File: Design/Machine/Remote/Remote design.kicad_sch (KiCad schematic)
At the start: 27 parts, among them SW1 PAuto, SW10 SyncRemote, SW11 PManual, SW12 YCardR, SW13 RCardR, SW14 IncPeriod, SW15 DecRight, SW16 IncRight, SW17 ThreeMin, SW18 DecTime, SW19 CycleTime, SW2 Block, SW20 PauseRes, SW21 Upload, SW3 YCardL, SW4 RCardL, SW5 DecLeft, SW6 IncLeft, SW7 OneMin, SW8 IncTime, SW9 ResetMachine

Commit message: fix: RF module PCB footprint
change RF module's PCB footprint
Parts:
- FS1000A1: footprint Connector_PinSocket_2.54mm:PinSocket_1x03_P2.54mm_Vertical -> Arduino_modules:FS1000A_Straight-Pins_Without-Headers
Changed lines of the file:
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@@
       (effects (font (size 1.27 1.27)) (justify left))
     )
-    (property "Footprint" "Connector_PinSocket_2.54mm:PinSocket_1x03_P2.54mm_Vertical" (at 254 104.14 0)
+    (property "Footprint" "Arduino_modules:FS1000A_Straight-Pins_Without-Headers" (at 254 104.14 0)
       (effects (font (size 1.27 1.27)) hide)
     )

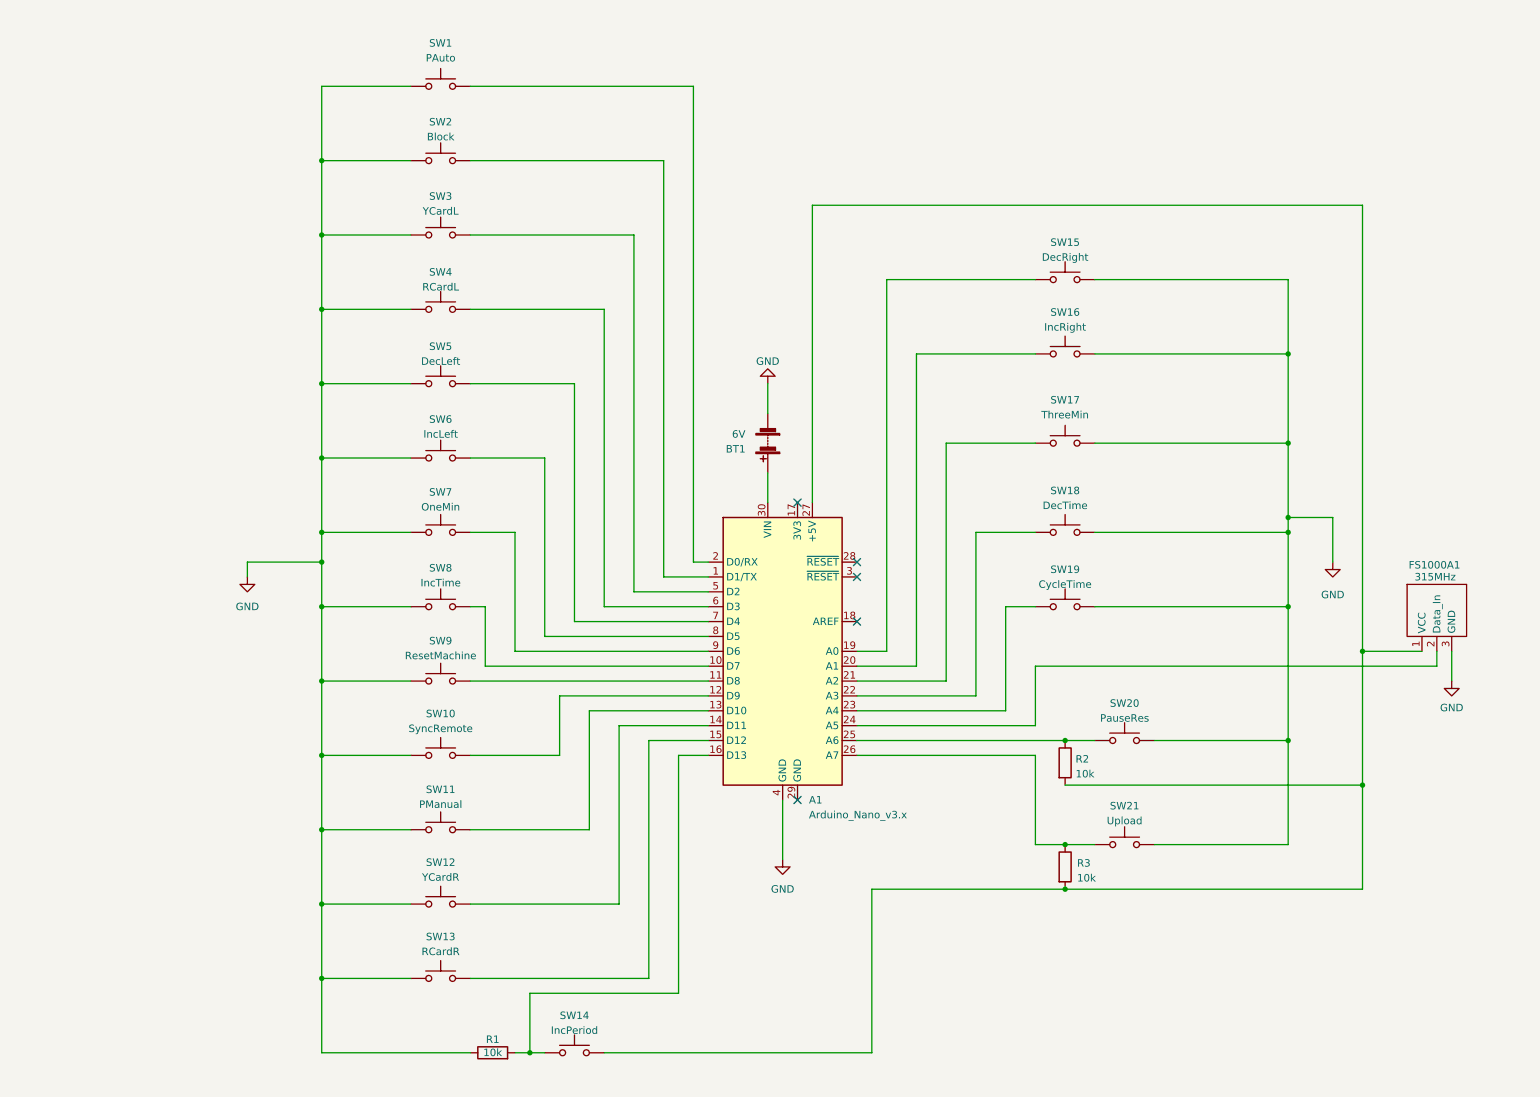
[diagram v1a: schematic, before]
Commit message: fix: controller schematic
fix controller's connections to GND and VCC, add SPST ON/OFF switch
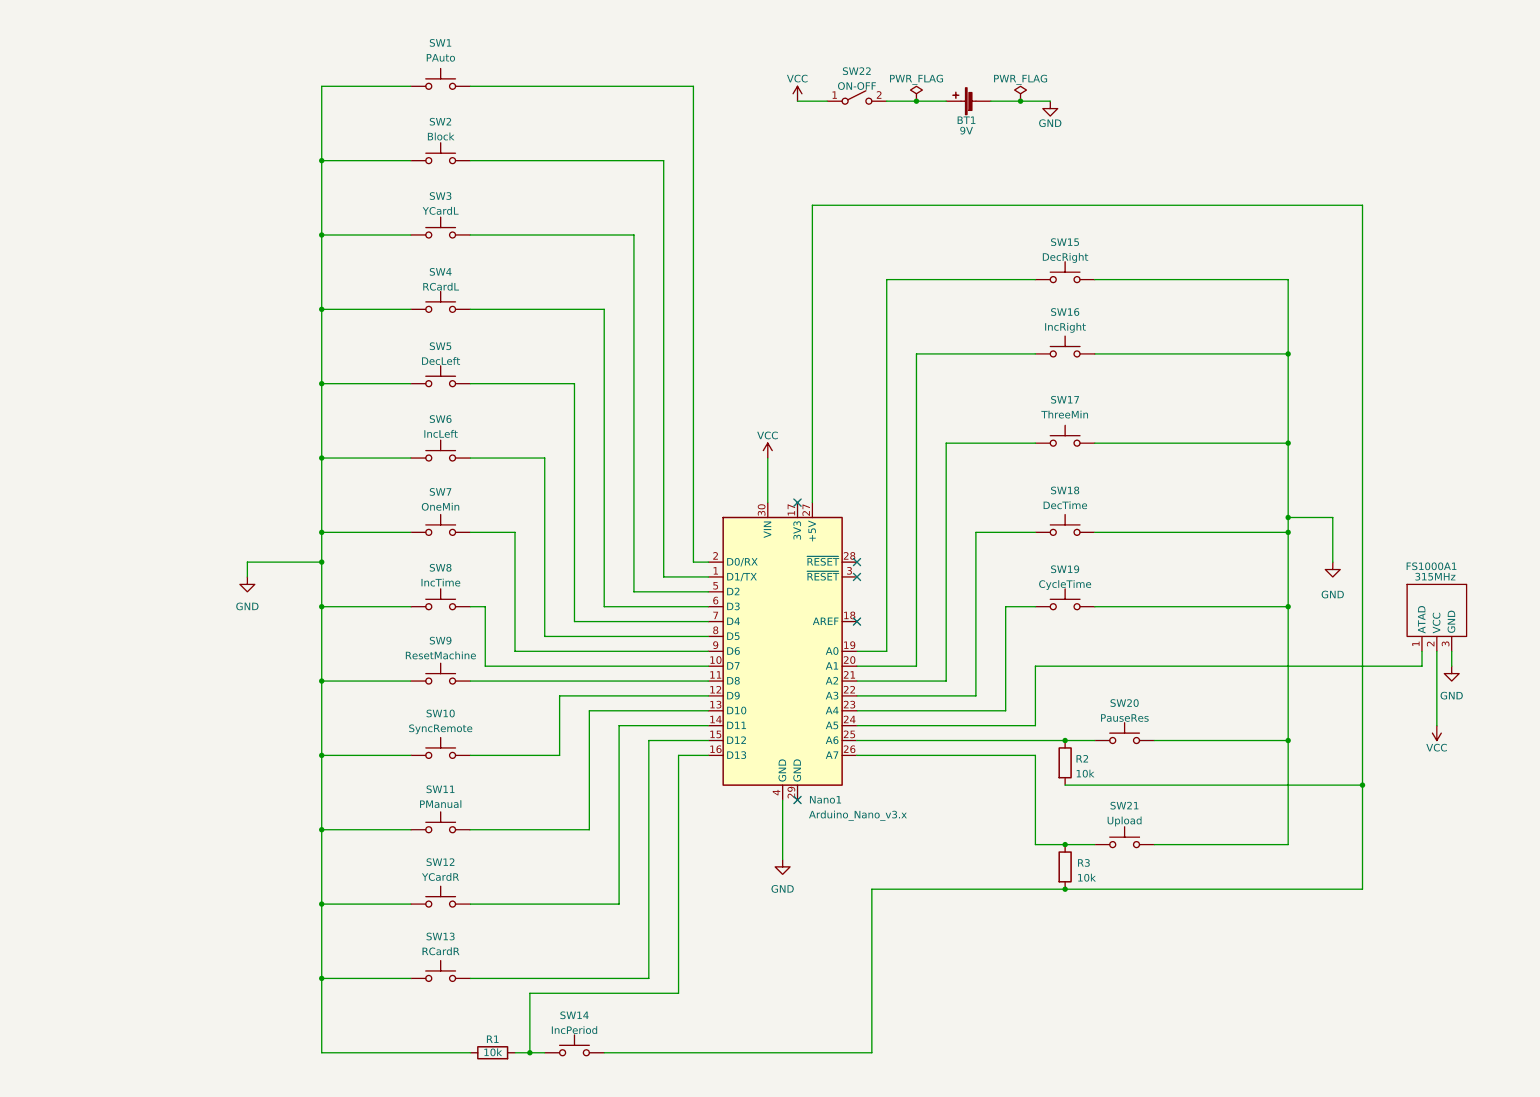
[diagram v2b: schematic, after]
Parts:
- removed BT1: 6V, Connector_PinSocket_2.54mm:PinSocket_1x02_P2.54mm_Vertical, symbol Device:Battery
- added BT1: 9V, Connector_PinHeader_2.54mm:PinHeader_1x02_P2.54mm_Vertical, symbol Device:Battery_Cell
- added SW22: ON-OFF, Connector_PinHeader_2.54mm:PinHeader_1x02_P2.54mm_Vertical, symbol Switch:SW_SPST
- renumbered A1 to Nano1
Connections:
- net GND: now also BT1.2 (-)
- net at Nano1.27 (+5V), R2.2, R3.2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: no longer FS1000A1.1 (VCC)
- net VCC: now reaches Nano1.30 (VIN)
- net VCC: now also FS1000A1.2 (VCC), SW22.1 (A)
- net at Nano1.24 (A5): now also FS1000A1.1 (ATAD); no longer FS1000A1.2 (Data_In)
- new net: BT1.1 (+), SW22.2 (B)

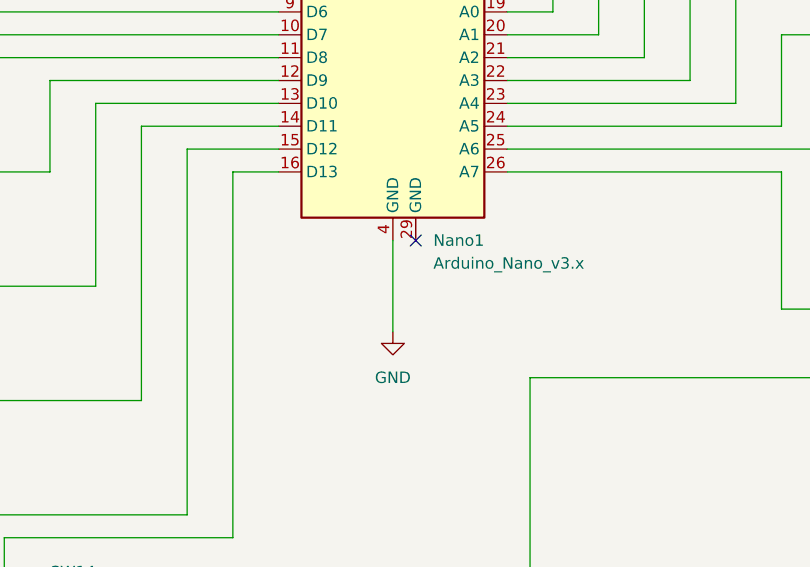
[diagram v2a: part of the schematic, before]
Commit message: fix: remote MCU GNDs
connect all Nano's GNDs to GND
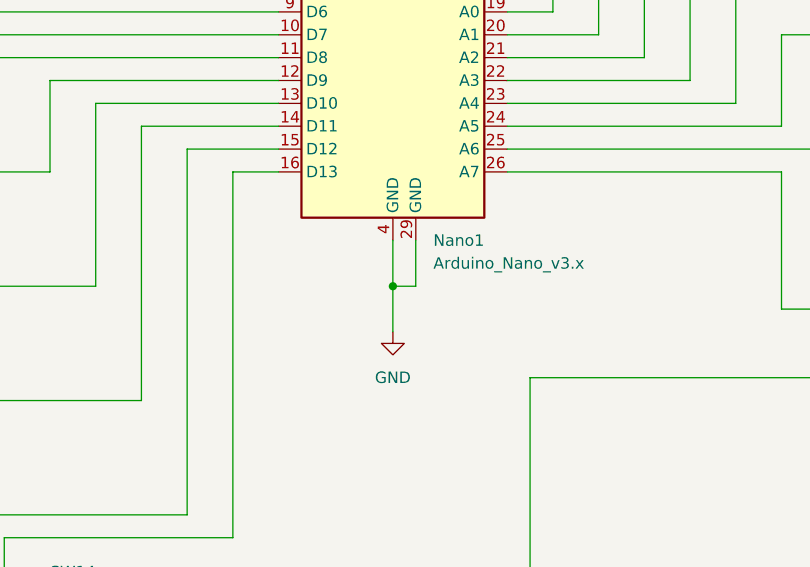
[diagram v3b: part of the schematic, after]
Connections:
- net GND: now also Nano1.29 (GND)
- no-connect marks 5 -> 4
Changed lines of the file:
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@@
   (junction (at 63.5 139.7) (diameter 0) (color 0 0 0 0)
+  )
+  (junction (at 142.24 152.4) (diameter 0) (color 0 0 0 0)
   )
   (junction (at 63.5 50.8) (diameter 0) (color 0 0 0 0)
@@
   (no_connect (at 154.94 116.84))
   (no_connect (at 154.94 106.68))
-  (no_connect (at 144.78 147.32))
   (no_connect (at 154.94 109.22))
   (no_connect (at 144.78 96.52))
@@
     (stroke (width 0) (type default))
   )
-  (wire (pts (xy 142.24 147.32) (xy 142.24 157.48))
+  (wire (pts (xy 142.24 147.32) (xy 142.24 152.4))
     (stroke (width 0) (type default))
   )
@@
     (stroke (width 0) (type default))
   )
+  (wire (pts (xy 142.24 152.4) (xy 142.24 157.48))
+    (stroke (width 0) (type default))
+  )
   (wire (pts (xy 63.5 127) (xy 63.5 139.7))
     (stroke (width 0) (type default))
@@
     (stroke (width 0) (type default))
   )
+  (wire (pts (xy 144.78 152.4) (xy 142.24 152.4))
+    (stroke (width 0) (type default))
+  )
   (wire (pts (xy 185.42 86.36) (xy 170.18 86.36))
     (stroke (width 0) (type default))
@@
     (stroke (width 0) (type default))
   )
+  (wire (pts (xy 144.78 147.32) (xy 144.78 152.4))
+    (stroke (width 0) (type default))
+  )

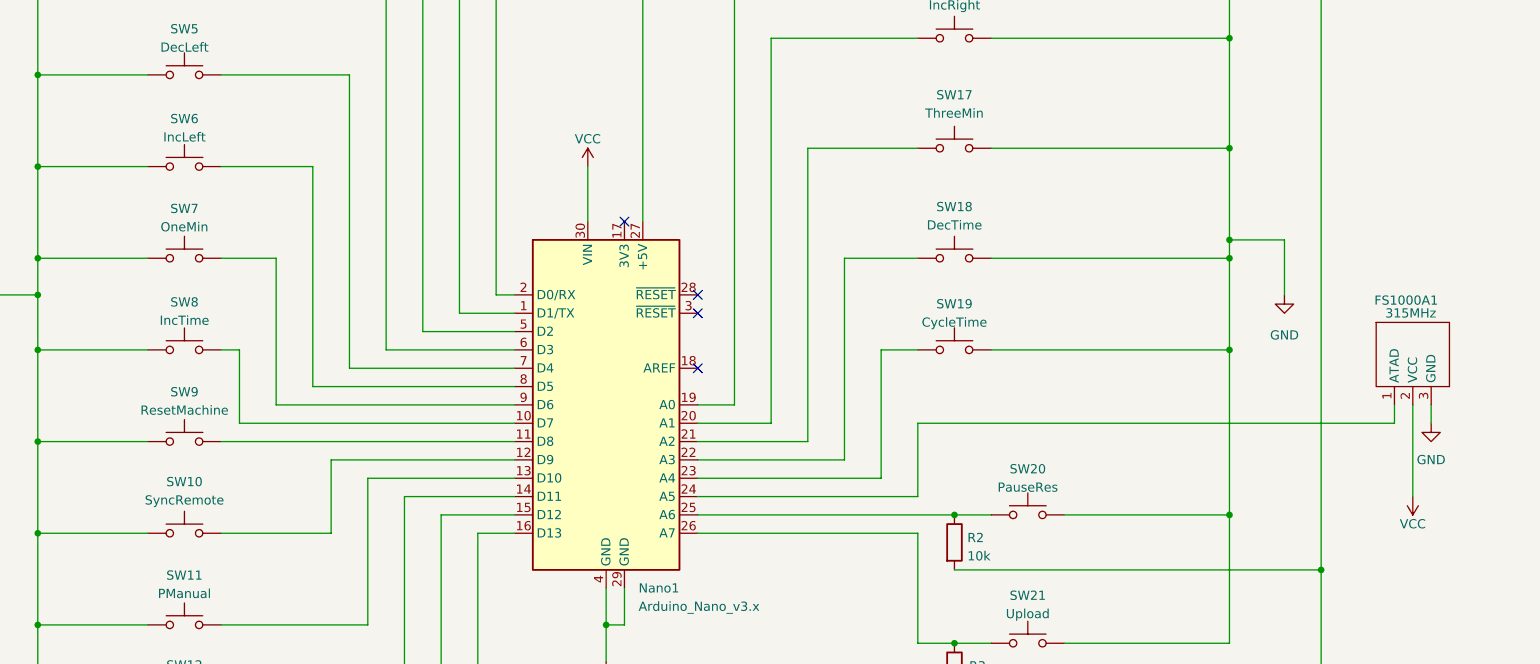
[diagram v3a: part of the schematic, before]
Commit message: feat: turn remote into Bluetooth remote
change code to make remote send data through BT
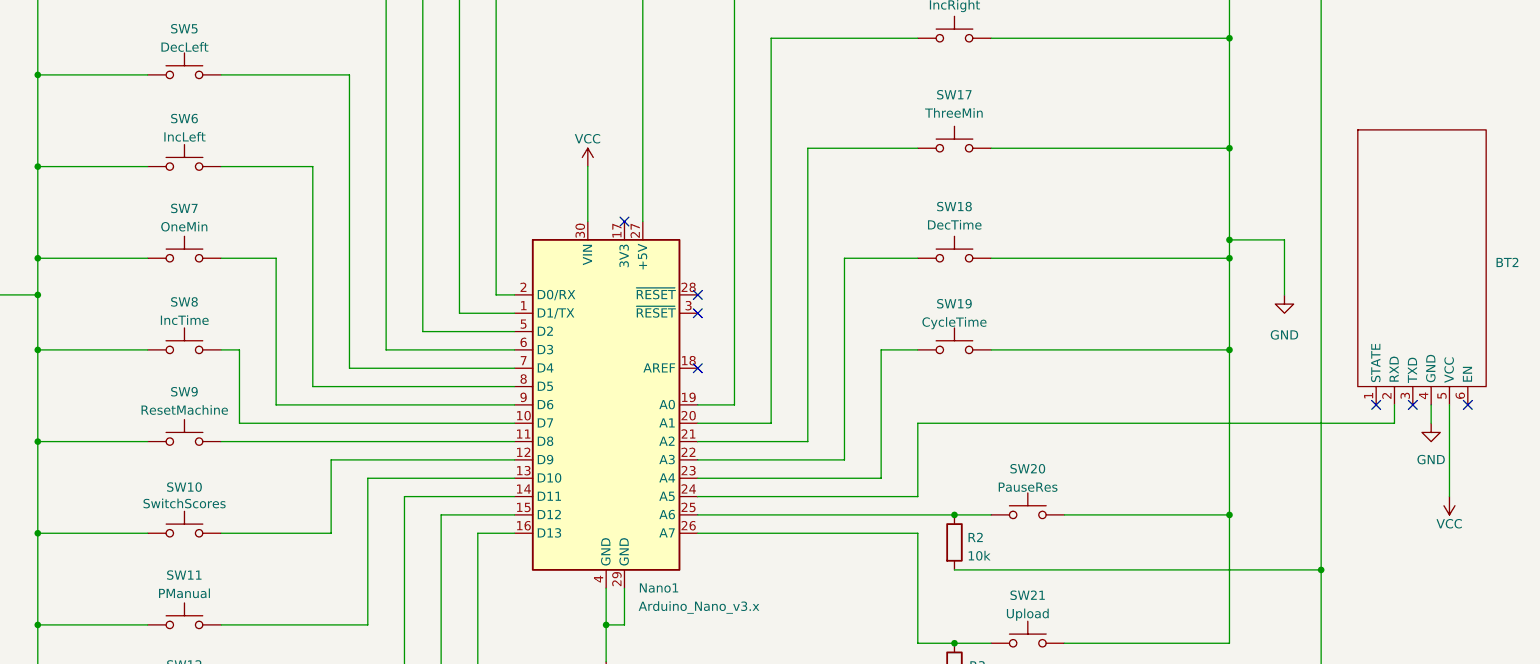
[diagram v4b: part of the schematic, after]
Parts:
- removed FS1000A1: 315MHz, Arduino_modules:FS1000A_Straight-Pins_Without-Headers, symbol Arduino modules:FS1000A
- added BT2: ~, symbol Arduino modules:ZS-040_HC-05
- SW10: value SyncRemote -> SwitchScores
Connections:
- net GND: now also BT2.4 (GND)
- net VCC: now also BT2.5 (VCC)
- net at Nano1.24 (A5): now also BT2.2 (RXD)
- no-connect marks 4 -> 7
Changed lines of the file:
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@@
   (junction (at 63.5 50.8) (diameter 0) (color 0 0 0 0)
   )
+  (no_connect (at 254 121.92))
+  (no_connect (at 261.62 121.92))
   (no_connect (at 154.94 116.84))
   (no_connect (at 154.94 106.68))
+  (no_connect (at 248.92 121.92))
   (no_connect (at 154.94 109.22))
   (no_connect (at 144.78 96.52))
@@
     (stroke (width 0) (type default))
   )
-  (wire (pts (xy 254 121.92) (xy 254 134.62))
+  (wire (pts (xy 259.08 121.92) (xy 259.08 134.62))
     (stroke (width 0) (type default))
   )
@@
     )
   )
-  (symbol (lib_id "Arduino modules:FS1000A") (at 254 110.49 0) (unit 1)
+  (symbol (lib_id "Arduino modules:ZS-040_HC-05") (at 254 83.82 0) (unit 1)
+    (in_bom yes) (on_board yes) (dnp no) (fields_autoplaced)
+    (property "Reference" "BT2" (at 265.43 102.235 0)
+      (effects (font (size 1.27 1.27)) (justify left))
+    )
+    (property "Value" "~" (at 254 83.82 0)
+      (effects (font (size 1.27 1.27)))
+    )
+    (property "Footprint" "" (at 254 83.82 0)
+      (effects (font (size 1.27 1.27)) hide)
+    )
+    (property "Datasheet" "" (at 254 83.82 0)
+      (effects (font (size 1.27 1.27)) hide)
+    )
+    (pin "1")
+    (pin "2")
+    (pin "3")
+    (pin "4")
+    (pin "5")
+    (pin "6")
+    (instances
+      (project "Remote design"
+        (path "/59847350-b8d0-4084-866f-18c46de7f096"
+          (reference "BT2") (unit 1)
+        )
+      )
+    )
+  )
+  (symbol (lib_id "Switch:SW_Push") (at 83.82 139.7 0) (unit 1)
     (in_bom yes) (on_board yes) (dnp no)
-    (property "Reference" "FS1000A1" (at 248.666 107.442 0)
-      (effects (font (size 1.27 1.27)) (justify left))
-    )
-    (property "Value" "315MHz" (at 250.19 109.22 0)
-      (effects (font (size 1.27 1.27)) (justify left))
-    )
-    (property "Footprint" "Arduino_modules:FS1000A_Straight-Pins_Without-Headers" (at 254 104.14 0)
-      (effects (font (size 1.27 1.27)) hide)
-    )
-    (property "Datasheet" "" (at 254 110.49 0)
-      (effects (font (size 1.27 1.27)) hide)
-    )
-    (pin "1")
-    (pin "2")
-    (pin "3")
-    (instances
-      (project "Remote design"
-        (path "/59847350-b8d0-4084-866f-18c46de7f096"
-          (reference "FS1000A1") (unit 1)
-        )
-      )
-    )
-  )
-  (symbol (lib_id "Switch:SW_Push") (at 83.82 139.7 0) (unit 1)
-    (in_bom yes) (on_board yes) (dnp no) (fields_autoplaced)
-    (property "Reference" "SW10" (at 83.82 132.588 0)
-      (effects (font (size 1.27 1.27)))
-    )
-    (property "Value" "SyncRemote" (at 83.82 135.128 0)
+    (property "Reference" "SW10" (at 83.82 133.35 0)
+      (effects (font (size 1.27 1.27)))
+    )
+    (property "Value" "SwitchScores" (at 83.82 135.636 0)
       (effects (font (size 1.27 1.27)))
     )
@@
     )
   )
-  (symbol (lib_id "power:VCC") (at 254 134.62 180) (unit 1)
-    (in_bom yes) (on_board yes) (dnp no) (fields_autoplaced)
-    (property "Reference" "#PWR07" (at 254 130.81 0)
-      (effects (font (size 1.27 1.27)) hide)
-    )
-    (property "Value" "VCC" (at 254 138.43 0)
-      (effects (font (size 1.27 1.27)))
-    )
-    (property "Footprint" "" (at 254 134.62 0)
-      (effects (font (size 1.27 1.27)) hide)
-    )
-    (property "Datasheet" "" (at 254 134.62 0)
-      (effects (font (size 1.27 1.27)) hide)
-    )
+  (symbol (lib_id "power:VCC") (at 259.08 134.62 180) (unit 1)
+    (in_bom yes) (on_board yes) (dnp no) (fields_autoplaced)
+    (property "Reference" "#PWR07" (at 259.08 130.81 0)
+      (effects (font (size 1.27 1.27)) hide)
+    )
+    (property "Value" "VCC" (at 259.08 138.43 0)
+      (effects (font (size 1.27 1.27)))
+    )
+    (property "Footprint" "" (at 259.08 134.62 0)
+      (effects (font (size 1.27 1.27)) hide)
+    )
+    (property "Datasheet" "" (at 259.08 134.62 0)
+      (effects (font (size 1.27 1.27)) hide)
+    )
